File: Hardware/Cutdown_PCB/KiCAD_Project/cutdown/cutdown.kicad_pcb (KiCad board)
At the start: 4 copper layers, 43.2 x 152.4 mm, 81 parts, among them J1 Mini_USB_B, J2 External Cutdown, J3 ISP, J4 Hot Wire, Q1 2N7002, Q2 FQP30N06L, SW1 SW_SPST, U1 FT231XS, U2 SPX3819M5-L-3-3, U3 ATmega328P-AU, U4 XBee, U5 BMP388, Y1 8MHz

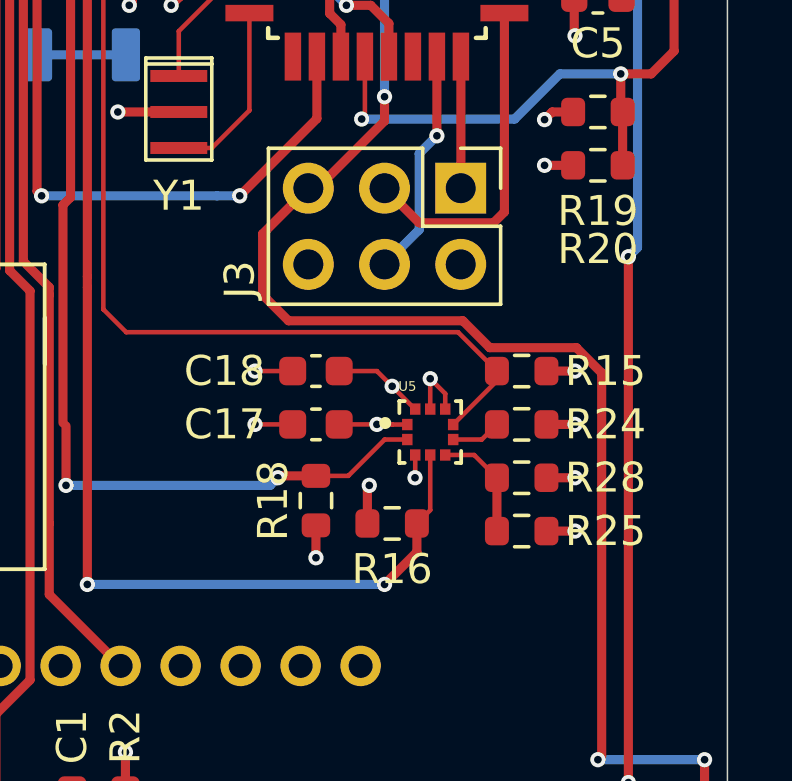
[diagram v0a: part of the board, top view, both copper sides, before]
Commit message: Create Rev 3.1 production files
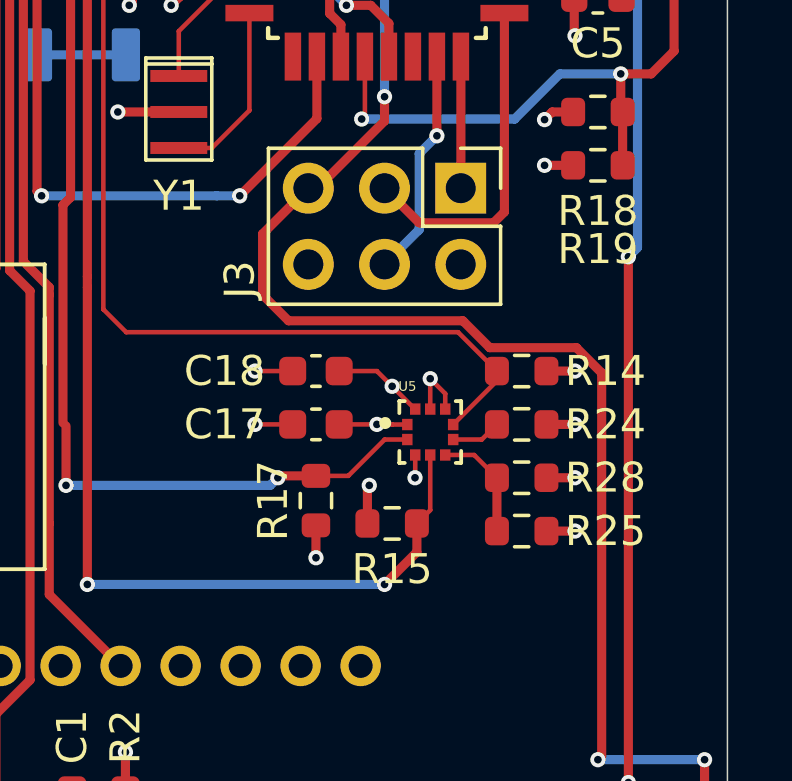
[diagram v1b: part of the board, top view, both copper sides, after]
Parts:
- renumbered D6 to D5, D5 to D6, R15 to R14, R16 to R15, R17 to R16, R18 to R17, R19 to R18, R20 to R19, R14 to R20
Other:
- board text added: "Cutdown Rev 3.1 3-0000106 7-0000062"
- board text removed: "Balloon Cutdown Rev 3.1 3-0000XXX"
